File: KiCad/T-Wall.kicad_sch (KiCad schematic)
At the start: 46 parts, among them J1 Conn_1, J2 Conn_2, J3 Conn_3, J4 Conn_4, J5 Conn_5, J6 Conn_6, J7 Conn_7, J8 Conn_8, J9 2086-1208/700-000/997-607, U1 TCA9555DBR, U2 TCA9555DBR, U3 TCA9555DBR, U4 TCA9555DBR, U5 ESP32-S3-DevKitC, U6 SN74AHCT125N, U7 LMZM23601V3

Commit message: changed KiCad libraries to project-specific libraries
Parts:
- J9: footprint 2086-1208_700-000_997-607:2086-1208_700-000_997-607 -> footprints:2086-1208_700-000_997-607
- U5: footprint PCM_Espressif:ESP32-S3-DevKitC -> footprints:ESP32-S3-DevKitC
- U6: footprint SN74AHCT125N:DIP794W45P254L1930H508Q14 -> footprints:SN74HCT125N
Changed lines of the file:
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@@
 			)
 		)
-		(property "Footprint" "SN74AHCT125N:DIP794W45P254L1930H508Q14"
+		(property "Footprint" "footprints:SN74HCT125N"
 			(at 274.32 166.37 0)
 			(effects
@@
 		)
 		(instances
-			(project ""
+			(project "T-Wall"
 				(path "/7dc9e5b9-dd7a-4571-90c7-051ff63df3d4"
 					(reference "U6")
@@
 			)
 		)
-		(property "Footprint" "2086-1208_700-000_997-607:2086-1208_700-000_997-607"
+		(property "Footprint" "footprints:2086-1208_700-000_997-607"
 			(at 271.78 68.58 0)
 			(effects
@@
 		)
 		(instances
-			(project ""
+			(project "T-Wall"
 				(path "/7dc9e5b9-dd7a-4571-90c7-051ff63df3d4"
 					(reference "J9")
@@
 		)
 		(instances
-			(project ""
+			(project "T-Wall"
 				(path "/7dc9e5b9-dd7a-4571-90c7-051ff63df3d4"
 					(reference "#PWR09")
@@
 		)
 		(instances
-			(project ""
+			(project "T-Wall"
 				(path "/7dc9e5b9-dd7a-4571-90c7-051ff63df3d4"
 					(reference "#PWR06")
@@
 		)
 		(instances
-			(project ""
+			(project "T-Wall"
 				(path "/7dc9e5b9-dd7a-4571-90c7-051ff63df3d4"
 					(reference "#PWR058")
@@
 		)
 		(instances
-			(project ""
+			(project "T-Wall"
 				(path "/7dc9e5b9-dd7a-4571-90c7-051ff63df3d4"
 					(reference "#PWR038")
@@
 		)
 		(instances
-			(project ""
+			(project "T-Wall"
 				(path "/7dc9e5b9-dd7a-4571-90c7-051ff63df3d4"
 					(reference "#PWR048")
@@
 		)
 		(instances
-			(project ""
+			(project "T-Wall"
 				(path "/7dc9e5b9-dd7a-4571-90c7-051ff63df3d4"
 					(reference "#PWR060")
@@
 		)
 		(instances
-			(project ""
+			(project "T-Wall"
 				(path "/7dc9e5b9-dd7a-4571-90c7-051ff63df3d4"
 					(reference "#PWR02")
@@
 		)
 		(instances
-			(project ""
+			(project "T-Wall"
 				(path "/7dc9e5b9-dd7a-4571-90c7-051ff63df3d4"
 					(reference "#PWR042")
@@
 		)
 		(instances
-			(project ""
+			(project "T-Wall"
 				(path "/7dc9e5b9-dd7a-4571-90c7-051ff63df3d4"
 					(reference "#PWR04")
@@
 		)
 		(instances
-			(project ""
+			(project "T-Wall"
 				(path "/7dc9e5b9-dd7a-4571-90c7-051ff63df3d4"
 					(reference "#PWR010")
@@
 		)
 		(instances
-			(project ""
+			(project "T-Wall"
 				(path "/7dc9e5b9-dd7a-4571-90c7-051ff63df3d4"
 					(reference "#PWR040")
@@
 		)
 		(instances
-			(project ""
+			(project "T-Wall"
 				(path "/7dc9e5b9-dd7a-4571-90c7-051ff63df3d4"
 					(reference "JP2")
@@
 		)
 		(instances
-			(project ""
+			(project "T-Wall"
 				(path "/7dc9e5b9-dd7a-4571-90c7-051ff63df3d4"
 					(reference "U7")
@@
 		)
 		(instances
-			(project ""
+			(project "T-Wall"
 				(path "/7dc9e5b9-dd7a-4571-90c7-051ff63df3d4"
 					(reference "#PWR03")
@@
 		)
 		(instances
-			(project ""
+			(project "T-Wall"
 				(path "/7dc9e5b9-dd7a-4571-90c7-051ff63df3d4"
 					(reference "C5")
@@
 		)
 		(instances
-			(project ""
+			(project "T-Wall"
 				(path "/7dc9e5b9-dd7a-4571-90c7-051ff63df3d4"
 					(reference "#PWR059")
@@
 		)
 		(instances
-			(project ""
+			(project "T-Wall"
 				(path "/7dc9e5b9-dd7a-4571-90c7-051ff63df3d4"
 					(reference "J2")
@@
 		)
 		(instances
-			(project ""
+			(project "T-Wall"
 				(path "/7dc9e5b9-dd7a-4571-90c7-051ff63df3d4"
 					(reference "#PWR044")
@@
 		)
 		(instances
-			(project ""
+			(project "T-Wall"
 				(path "/7dc9e5b9-dd7a-4571-90c7-051ff63df3d4"
 					(reference "#PWR052")
@@
 		)
 		(instances
-			(project ""
+			(project "T-Wall"
 				(path "/7dc9e5b9-dd7a-4571-90c7-051ff63df3d4"
 					(reference "#PWR050")
@@
 		)
 		(instances
-			(project ""
+			(project "T-Wall"
 				(path "/7dc9e5b9-dd7a-4571-90c7-051ff63df3d4"
 					(reference "#PWR046")
@@
 		)
 		(instances
-			(project ""
+			(project "T-Wall"
 				(path "/7dc9e5b9-dd7a-4571-90c7-051ff63df3d4"
 					(reference "C1")
@@
 			)
 		)
-		(property "Footprint" "PCM_Espressif:ESP32-S3-DevKitC"
+		(property "Footprint" "footprints:ESP32-S3-DevKitC"
 			(at 222.25 24.13 0)
 			(effects
@@
 		)
 		(instances
-			(project ""
+			(project "T-Wall"
 				(path "/7dc9e5b9-dd7a-4571-90c7-051ff63df3d4"
 					(reference "U5")
@@
 		)
 		(instances
-			(project ""
+			(project "T-Wall"
 				(path "/7dc9e5b9-dd7a-4571-90c7-051ff63df3d4"
 					(reference "R8")
@@
 		)
 		(instances
-			(project ""
+			(project "T-Wall"
 				(path "/7dc9e5b9-dd7a-4571-90c7-051ff63df3d4"
 					(reference "U1")
@@
 		)
 		(instances
-			(project ""
+			(project "T-Wall"
 				(path "/7dc9e5b9-dd7a-4571-90c7-051ff63df3d4"
 					(reference "JP1")
@@
 		)
 		(instances
-			(project ""
+			(project "T-Wall"
 				(path "/7dc9e5b9-dd7a-4571-90c7-051ff63df3d4"
 					(reference "#PWR01")

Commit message: just some BWL things...
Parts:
- removed J9: 2086-1208/700-000/997-607, footprints:2086-1208_700-000_997-607, symbol 2068-1208_700-000_997-607:2086-1208_700-000_997-607
- removed U6: SN74AHCT125N, footprints:SN74HCT125N, symbol SN74AHCT125N:SN74AHCT125N
- added J9: 2086-1107/300-000/997-607, footprints:2086-1107_300-000_997-607, symbol symbols:2086-1107_300-000_997-607
- added U8: SN74AHCT125RGYR, footprints:SN74AHCT125RGYR, symbol symbols:SN74AHCT125RGYR
- C5, C6: LCSC C96446 -> C13585
- J1: value Conn_1 -> IDC; now fitted
- J2: value Conn_2 -> IDC; now fitted
- J3: value Conn_3 -> IDC; now fitted
- J4: value Conn_4 -> IDC; now fitted
- J5: value Conn_5 -> IDC; now fitted
- J6: value Conn_6 -> IDC; now fitted
- J7: value Conn_7 -> IDC; now fitted
- J8: value Conn_8 -> IDC; now fitted
- U7: LCSC (none) -> C2864948
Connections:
- net +5V: now also J9.6_1, J9.6_2, U8.14 (VCC)
- net GND: now also J9.7_1, J9.7_2, U8.15 (EPAD), U8.7 (GND)
- net LEDS_DATA_EN: now also U8.1 (*1OE), U8.10 (*3OE), U8.13 (*4OE), U8.4 (*2OE)
- net LEDS_GPIO_1: now also U8.2 (1A)
- net LEDS_GPIO_2: now also U8.5 (2A)
- net LEDS_GPIO_3: now also U5.18 (GPIO12/ADC2_CH1), U8.9 (3A); no longer U5.19 (GPIO13/ADC2_CH2)
- net LEDS_GPIO_4: now also U5.19 (GPIO13/ADC2_CH2), U8.12 (4A); no longer U5.18 (GPIO12/ADC2_CH1)
- net LEDS_OUT_1: now also R3.2, J9.1_1, J9.1_2; no longer R3.1
- net LEDS_OUT_2: now also R10.2, J9.2_1, J9.2_2; no longer R10.1
- net LEDS_OUT_3: now also J9.3_1, J9.3_2
- net LEDS_OUT_4: now also J9.4_1, J9.4_2
- net LEDS_PWR_EN: now also J9.5_1, J9.5_2
- net at R12.2: now also U8.11 (4Y)
- net at R11.2: now also U8.8 (3Y)
- new net: R10.1, U8.6 (2Y)
- new net: R3.1, U8.3 (1Y)
- no-connect marks 26 -> 24
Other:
- moved on the sheet: R10, R11, R12, R3

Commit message: Finished BWL-rebuild
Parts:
- removed C6: 10u, Capacitor_SMD:C_1206_3216Metric_Pad1.33x1.80mm_HandSolder, symbol Device:C
- removed R8, R9: 10k, Resistor_SMD:R_0402_1005Metric_Pad0.72x0.64mm_HandSolder, symbol Device:R_Small
- removed U1, U2, U3, U4: TCA9555DBR, Package_SO:SSOP-24_5.3x8.2mm_P0.65mm, symbol Interface_Expansion:TCA9555DBR
- removed U5: ESP32-S3-DevKitC, footprints:ESP32-S3-DevKitC, symbol Espressif:ESP32-S3-DevKitC
- removed U7: LMZM23601V3, Package_LGA:Texas_SIL0010A_MicroSiP-10-1EP_3.8x3mm_P0.6mm_EP0.7x2.9mm_ThermalVias, symbol Regulator_Switching:LMZM23601V3
- added C7, C8: 10u, Capacitor_SMD:C_1206_3216Metric_Pad1.33x1.80mm_HandSolder, symbol Device:C
- added L1: 1u, Inductor_SMD:L_0805_2012Metric_Pad1.05x1.20mm_HandSolder, symbol Device:L
- added R13, R14: 10k, Resistor_SMD:R_0402_1005Metric_Pad0.72x0.64mm_HandSolder, symbol Device:R_Small
- added R15: 470k, Resistor_SMD:R_0201_0603Metric_Pad0.64x0.40mm_HandSolder, symbol Device:R
- added R16: 100k, Resistor_SMD:R_0201_0603Metric_Pad0.64x0.40mm_HandSolder, symbol Device:R
- added R17: 4.7k, Resistor_SMD:R_0402_1005Metric_Pad0.72x0.64mm_HandSolder, symbol Device:R
- added U1, U2, U3, U4: TCA9555PWR, Package_SO:TSSOP-24_4.4x7.8mm_P0.65mm, symbol Interface_Expansion:TCA9555PWR
- added U5: ESP32-S3-DevKitC, footprints:ESP32-S3-DevKitC, symbol symbols:ESP32-S3-DevKitC
- added U9: TPS62A01APDDC, Package_TO_SOT_SMD:SOT-23-6, symbol Regulator_Switching:TPS62A01APDDC
- renumbered U8 to U6
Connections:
- net +3.3V: now also C5.2, C8.2, L1.2, R14.1, R15.1, U1.24 (VCC), U2.24 (VCC), U3.24 (VCC), U4.24 (VCC)
- net +5V: now also C7.2, U5.21 (5V), U9.4 (VIN); no longer C5.2
- net DCDC_EN: now also R13.1, U5.40 (GPIO2/ADC1_CH1), U9.1 (EN)
- net DCDC_PGood: now also R14.2, U5.41 (GPIO1/ADC1_CH0), U9.5 (PG)
- net GND: now also C7.1, C8.1, R13.2, R17.2, U1.12 (GND), U2.12 (GND), U3.12 (GND), U4.12 (GND), U5.22 (GND), U5.23 (GND), U5.24 (GND), U5.44 (GND), U9.2 (GND)
- net I2C_SCL: now also U1.22 (SCL), U2.22 (SCL), U3.22 (SCL), U4.22 (SCL), U5.15 (GPIO9/ADC1_CH8)
- net I2C_SDA: now also U1.23 (SDA), U2.23 (SDA), U3.23 (SDA), U4.23 (SDA), U5.12 (GPIO8/ADC1_CH7)
- net INT_000: now also U1.1 (~{INT}), U5.4 (GPIO4/ADC1_CH3)
- net INT_001: now also U2.1 (~{INT}), U5.5 (GPIO5/ADC1_CH4)
- net INT_010: now also U3.1 (~{INT}), U5.6 (GPIO6/ADC1_CH5)
- net INT_011: now also U4.1 (~{INT}), U5.7 (GPIO7/ADC1_CH6)
- net LEDS_DATA_EN: now also U5.28 (GPIO47)
- net LEDS_GPIO_1: now also U5.16 (GPIO10/ADC1_CH9)
- net LEDS_GPIO_2: now also U5.17 (GPIO11/ADC2_CH0)
- net LEDS_GPIO_3: now also U5.18 (GPIO12/ADC2_CH1)
- net LEDS_GPIO_4: now also U5.19 (GPIO13/ADC2_CH2)
- net LEDS_PWR_EN: now also U5.29 (GPIO48)
- net Sensor_R1S1: now also U1.4 (P00)
- net Sensor_R1S2: now also U1.5 (P01)
- net Sensor_R1S3: now also U1.6 (P02)
- net Sensor_R1S4: now also U1.7 (P03)
- net Sensor_R1S5: now also U1.8 (P04)
- net Sensor_R1S6: now also U1.9 (P05)
- net Sensor_R1S7: now also U1.10 (P06)
- net Sensor_R1S8: now also U1.11 (P07)
- net Sensor_R2S1: now also U1.13 (P10)
- net Sensor_R2S2: now also U1.14 (P11)
- net Sensor_R2S3: now also U1.15 (P12)
- net Sensor_R2S4: now also U1.16 (P13)
- net Sensor_R2S5: now also U1.17 (P14)
- net Sensor_R2S6: now also U1.18 (P15)
- net Sensor_R2S7: now also U1.19 (P16)
- net Sensor_R2S8: now also U1.20 (P17)
- net Sensor_R3S1: now also U2.4 (P00)
- net Sensor_R3S2: now also U2.5 (P01)
- net Sensor_R3S3: now also U2.6 (P02)
- net Sensor_R3S4: now also U2.7 (P03)
- net Sensor_R3S5: now also U2.8 (P04)
- net Sensor_R3S6: now also U2.9 (P05)
- net Sensor_R3S7: now also U2.10 (P06)
- net Sensor_R3S8: now also U2.11 (P07)
- net Sensor_R4S1: now also U2.13 (P10)
- net Sensor_R4S2: now also U2.14 (P11)
- net Sensor_R4S3: now also U2.15 (P12)
- net Sensor_R4S4: now also U2.16 (P13)
- net Sensor_R4S5: now also U2.17 (P14)
- net Sensor_R4S6: now also U2.18 (P15)
- net Sensor_R4S7: now also U2.19 (P16)
- net Sensor_R4S8: now also U2.20 (P17)
- net Sensor_R5S1: now also U3.4 (P00)
- net Sensor_R5S2: now also U3.5 (P01)
- net Sensor_R5S3: now also U3.6 (P02)
- net Sensor_R5S4: now also U3.7 (P03)
- net Sensor_R5S5: now also U3.8 (P04)
- net Sensor_R5S6: now also U3.9 (P05)
- net Sensor_R5S7: now also U3.10 (P06)
- net Sensor_R5S8: now also U3.11 (P07)
- net Sensor_R6S1: now also U3.13 (P10)
- net Sensor_R6S2: now also U3.14 (P11)
- net Sensor_R6S3: now also U3.15 (P12)
- net Sensor_R6S4: now also U3.16 (P13)
- net Sensor_R6S5: now also U3.17 (P14)
- net Sensor_R6S6: now also U3.18 (P15)
- net Sensor_R6S7: now also U3.19 (P16)
- net Sensor_R6S8: now also U3.20 (P17)
- net Sensor_R7S1: now also U4.4 (P00)
- net Sensor_R7S2: now also U4.5 (P01)
- net Sensor_R7S3: now also U4.6 (P02)
- net Sensor_R7S4: now also U4.7 (P03)
- net Sensor_R7S5: now also U4.8 (P04)
- net Sensor_R7S6: now also U4.9 (P05)
- net Sensor_R7S7: now also U4.10 (P06)
- net Sensor_R7S8: now also U4.11 (P07)
- net Sensor_R8S1: now also U4.13 (P10)
- net Sensor_R8S2: now also U4.14 (P11)
- net Sensor_R8S3: now also U4.15 (P12)
- net Sensor_R8S4: now also U4.16 (P13)
- net Sensor_R8S5: now also U4.17 (P14)
- net Sensor_R8S6: now also U4.18 (P15)
- net Sensor_R8S7: now also U4.19 (P16)
- net Sensor_R8S8: now also U4.20 (P17)
- net at JP0.2 (C): now also U1.21 (A0)
- net at JP10.2 (C): now also U4.2 (A1)
- net at JP9.2 (C): now also U4.21 (A0)
- net at JP11.2 (C): now also U4.3 (A2)
- net at JP4.2 (C): now also U2.2 (A1)
- net at JP3.2 (C): now also U2.21 (A0)
- net at JP5.2 (C): now also U2.3 (A2)
- net at JP8.2 (C): now also U3.3 (A2)
- net at JP7.2 (C): now also U3.2 (A1)
- net at JP6.2 (C): now also U3.21 (A0)
- net at JP2.2 (C): now also U1.3 (A2)
- net at JP1.2 (C): now also U1.2 (A1)
- new net: L1.1, U9.3 (SW)
- new net: R15.2, R16.1, U9.6 (FB)
- new net: R16.2, R17.1
- new net: U5.1 (3V3), U5.2 (3V3)

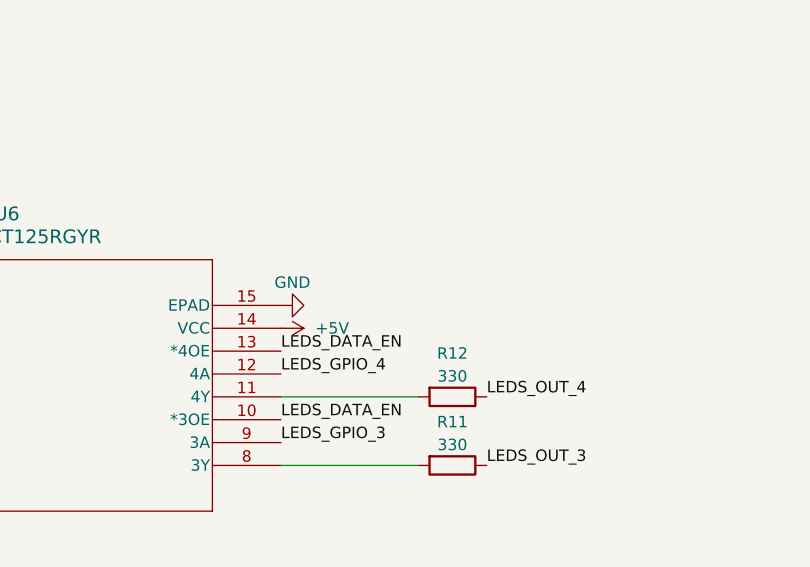
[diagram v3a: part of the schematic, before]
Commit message: added 100 nF capacitor for the level-shifter
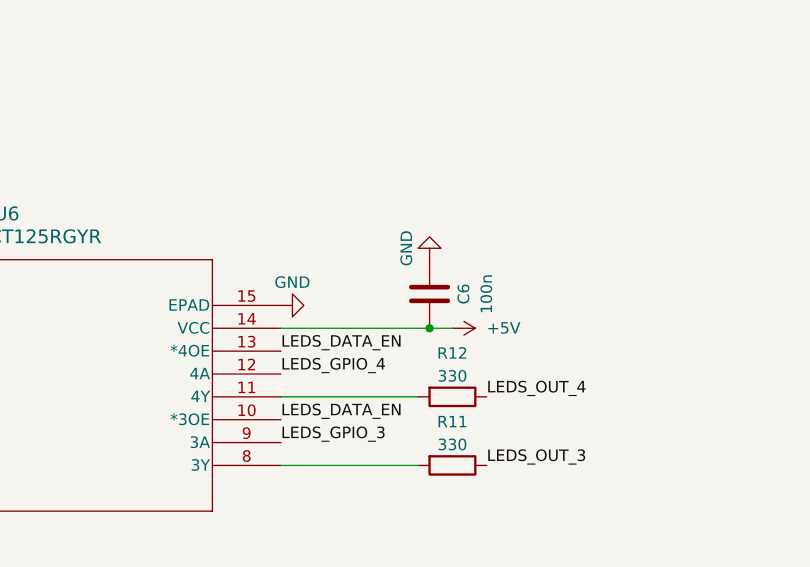
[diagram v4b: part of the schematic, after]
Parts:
- added C6: 100n, Capacitor_SMD:C_0402_1005Metric_Pad0.74x0.62mm_HandSolder, symbol Device:C
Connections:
- net +5V: now also C6.2
- net GND: now also C6.1
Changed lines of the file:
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@@
 	)
 	(junction
+		(at 320.04 147.32)
+		(diameter 0)
+		(color 0 0 0 0)
+	)
+	(junction
 		(at 142.24 231.14)
 		(diameter 0)
@@
 	(wire
 		(pts
+			(xy 322.58 147.32) (xy 320.04 147.32)
+		)
+		(stroke
+			(width 0)
+			(type default)
+		)
+	)
+	(wire
+		(pts
 			(xy 111.76 158.75) (xy 119.38 158.75)
 		)
@@
 	(wire
 		(pts
+			(xy 320.04 147.32) (xy 303.53 147.32)
+		)
+		(stroke
+			(width 0)
+			(type default)
+		)
+	)
+	(wire
+		(pts
 			(xy 93.98 88.9) (xy 93.98 85.09)
 		)
@@
 	(symbol
 		(lib_id "power:+5V")
-		(at 303.53 147.32 270)
+		(at 322.58 147.32 270)
 		(unit 1)
 		(exclude_from_sim no)
@@
 		(fields_autoplaced yes)
 		(property "Reference" "#PWR010"
-			(at 299.72 147.32 0)
+			(at 318.77 147.32 0)
 			(effects
 				(font
@@
 		)
 		(property "Value" "+5V"
-			(at 307.34 147.3199 90)
+			(at 326.39 147.3199 90)
 			(effects
 				(font
@@
 		)
 		(property "Footprint" ""
-			(at 303.53 147.32 0)
+			(at 322.58 147.32 0)
 			(effects
 				(font
@@
 		)
 		(property "Datasheet" ""
-			(at 303.53 147.32 0)
+			(at 322.58 147.32 0)
 			(effects
 				(font
@@
 		)
 		(property "Description" "Power symbol creates a global label with name \"+5V\""
-			(at 303.53 147.32 0)
+			(at 322.58 147.32 0)
 			(effects
 				(font
@@
 	)
 	(symbol
+		(lib_id "Device:C")
+		(at 320.04 143.51 0)
+		(unit 1)
+		(exclude_from_sim no)
+		(in_bom yes)
+		(on_board yes)
+		(dnp no)
+		(property "Reference" "C6"
+			(at 323.85 143.51 90)
+			(effects
+				(font
+					(size 1.27 1.27)
+				)
+			)
+		)
+		(property "Value" "100n"
+			(at 326.39 143.51 90)
+			(effects
+				(font
+					(size 1.27 1.27)
+				)
+			)
+		)
+		(property "Footprint" "Capacitor_SMD:C_0402_1005Metric_Pad0.74x0.62mm_HandSolder"
+			(at 321.0052 147.32 0)
+			(effects
+				(font
+					(size 1.27 1.27)
+				)
+				(hide yes)
+			)
+		)
+		(property "Datasheet" "~"
+			(at 320.04 143.51 0)
+			(effects
+				(font
+					(size 1.27 1.27)
+				)
+				(hide yes)
+			)
+		)
+		(property "Description" "Unpolarized capacitor"
+			(at 320.04 143.51 0)
+			(effects
+				(font
+					(size 1.27 1.27)
+				)
+				(hide yes)
+			)
+		)
+		(property "LCSC" "C1525"
+			(at 320.04 143.51 90)
+			(effects
+				(font
+					(size 1.27 1.27)
+				)
+				(hide yes)
+			)
+		)
+		(pin "1"
+		)
+		(pin "2"
+		)
+		(instances
+			(project "T-Wall"
+				(path "/7dc9e5b9-dd7a-4571-90c7-051ff63df3d4"
+					(reference "C6")
+					(unit 1)
+				)
+			)
+		)
+	)
+	(symbol
 		(lib_id "power:GND")
 		(at 242.57 160.02 270)
@@
 					(unit 1)
 				)
+			)
+		)
+	)
+	(symbol
+		(lib_id "power:GND")
+		(at 320.04 139.7 180)
+		(unit 1)
+		(exclude_from_sim no)
+		(in_bom yes)
+		(on_board yes)
+		(dnp no)
+		(property "Reference" "#PWR036"
+			(at 320.04 133.35 0)
+			(effects
+				(font
+					(size 1.27 1.27)
+				)
+				(hide yes)
+			)
+		)
+		(property "Value" "GND"
+			(at 317.5 138.43 90)
+			(effects
+				(font
+					(size 1.27 1.27)
+				)
+			)
+		)
+		(property "Footprint" ""
+			(at 320.04 139.7 0)
+			(effects
+				(font
+					(size 1.27 1.27)
+				)
+				(hide yes)
+			)
+		)
+		(property "Datasheet" ""
+			(at 320.04 139.7 0)
+			(effects
+				(font
+					(size 1.27 1.27)
+				)
+				(hide yes)
+			)
+		)
+		(property "Description" "Power symbol creates a global label with name \"GND\" , ground"
+			(at 320.04 139.7 0)
+			(effects
+				(font
+					(size 1.27 1.27)
+				)
+				(hide yes)
+			)
+		)
+		(pin "1"
+		)
+		(instances
+			(project "T-Wall"
+				(path "/7dc9e5b9-dd7a-4571-90c7-051ff63df3d4"
+					(reference "#PWR036")
+					(unit 1)
+				)
